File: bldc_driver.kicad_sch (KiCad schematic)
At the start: 100 parts, among them IC1 STSPIN32G4, IC2 AS5047D-ATSM, J2 Conn_01x02_Pin, J3 Conn_01x02_Pin, J4 Conn_01x05_Pin, J4 ST-Link, P1 USB_C_Plug_USB2.0, Q1 NMOS, Q2 NMOS, Q3 NMOS, Q4 NMOS, Q5 NMOS, Q6 NMOS, U1 TCAN332, U2 NJW1933, Y201 Crystal_GND24

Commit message: フットプリント割り当て中
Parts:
- added C3: 10u, Capacitor_SMD:C_1206_3216Metric_Pad1.33x1.80mm_HandSolder, symbol Device:C
- C1: renamed from C7; footprint (none) -> Capacitor_SMD:C_1206_3216Metric_Pad1.33x1.80mm_HandSolder
- C10: renamed from C1; footprint (none) -> Capacitor_SMD:C_0603_1608Metric_Pad1.08x0.95mm_HandSolder
- C11: renamed from C15; footprint (none) -> Capacitor_SMD:C_0603_1608Metric_Pad1.08x0.95mm_HandSolder
- C12: renamed from C2; footprint (none) -> Capacitor_SMD:C_0603_1608Metric_Pad1.08x0.95mm_HandSolder
- C13: renamed from C3; footprint (none) -> Capacitor_SMD:C_0603_1608Metric_Pad1.08x0.95mm_HandSolder
- C14: renamed from C16; footprint (none) -> Capacitor_SMD:C_0603_1608Metric_Pad1.08x0.95mm_HandSolder
- C15: renamed from C10; footprint (none) -> Capacitor_SMD:C_0603_1608Metric_Pad1.08x0.95mm_HandSolder
- C16: renamed from C9; footprint (none) -> Capacitor_SMD:C_0603_1608Metric_Pad1.08x0.95mm_HandSolder
- C17: renamed from C11; footprint (none) -> Capacitor_SMD:C_0603_1608Metric_Pad1.08x0.95mm_HandSolder
- C18: renamed from C12; footprint (none) -> Capacitor_SMD:C_0603_1608Metric_Pad1.08x0.95mm_HandSolder
- C19: renamed from C26; value 1n -> 2.2n; footprint (none) -> Capacitor_SMD:C_0603_1608Metric_Pad1.08x0.95mm_HandSolder
- C2: renamed from C8; footprint (none) -> Capacitor_SMD:C_1206_3216Metric_Pad1.33x1.80mm_HandSolder
- C20: renamed from C27; value 1n -> 2.2n; footprint (none) -> Capacitor_SMD:C_0603_1608Metric_Pad1.08x0.95mm_HandSolder
- C21: renamed from C28; value 1n -> 2.2n; footprint (none) -> Capacitor_SMD:C_0603_1608Metric_Pad1.08x0.95mm_HandSolder
- C22: renamed from C29; value 1n -> 2.2n; footprint (none) -> Capacitor_SMD:C_0603_1608Metric_Pad1.08x0.95mm_HandSolder
- C23: renamed from C30; value 1n -> 2.2n; footprint (none) -> Capacitor_SMD:C_0603_1608Metric_Pad1.08x0.95mm_HandSolder
- C24: renamed from C31; value 1n -> 2.2n; footprint (none) -> Capacitor_SMD:C_0603_1608Metric_Pad1.08x0.95mm_HandSolder
- C25: renamed from C17; footprint (none) -> Capacitor_SMD:C_0603_1608Metric_Pad1.08x0.95mm_HandSolder
- C26: renamed from C20; footprint (none) -> Capacitor_SMD:C_0603_1608Metric_Pad1.08x0.95mm_HandSolder
- C27: renamed from C21; footprint (none) -> Capacitor_SMD:C_0603_1608Metric_Pad1.08x0.95mm_HandSolder
- C28: renamed from C22; footprint (none) -> Capacitor_SMD:C_0603_1608Metric_Pad1.08x0.95mm_HandSolder
- C29: renamed from C23; footprint (none) -> Capacitor_SMD:CP_Elec_10x10
- C30: renamed from C24; footprint (none) -> Capacitor_SMD:CP_Elec_10x10
- C31: renamed from C25; footprint (none) -> Capacitor_SMD:CP_Elec_10x10
- C32: renamed from C19; footprint (none) -> Capacitor_SMD:C_0603_1608Metric_Pad1.08x0.95mm_HandSolder
- C34: footprint Capacitor_SMD:C_0603_1608Metric_Pad1.08x0.95mm_HandSolder -> Capacitor_SMD:C_0402_1005Metric_Pad0.74x0.62mm_HandSolder
- C4: renamed from C14; footprint (none) -> Capacitor_SMD:C_0603_1608Metric_Pad1.08x0.95mm_HandSolder
- C5: renamed from C32; footprint (none) -> Capacitor_SMD:C_0603_1608Metric_Pad1.08x0.95mm_HandSolder
- C6: renamed from C5; footprint (none) -> Capacitor_SMD:C_1206_3216Metric_Pad1.33x1.80mm_HandSolder
- C7: renamed from C4; footprint (none) -> Capacitor_SMD:C_0603_1608Metric_Pad1.08x0.95mm_HandSolder
- C8: renamed from C6; footprint (none) -> Capacitor_SMD:C_0603_1608Metric_Pad1.08x0.95mm_HandSolder
- C9: renamed from C13; footprint (none) -> Capacitor_SMD:C_0603_1608Metric_Pad1.08x0.95mm_HandSolder
- D1: footprint (none) -> sam:RSX101VAM
- D2: renamed from D3; footprint (none) -> Diode_SMD:D_0603_1608Metric_Pad1.05x0.95mm_HandSolder
- D3: renamed from D4; footprint (none) -> Diode_SMD:D_0603_1608Metric_Pad1.05x0.95mm_HandSolder
- D4: renamed from D5; footprint (none) -> Diode_SMD:D_0603_1608Metric_Pad1.05x0.95mm_HandSolder
- D5: renamed from D6; footprint (none) -> Diode_SMD:D_0603_1608Metric_Pad1.05x0.95mm_HandSolder
- IC1: footprint QFN50P900X900X100-65N-D -> stspin32g4:QFN50P900X900X100-65N-D
- IC2: footprint SOP65P640X120-14N -> as5047:SOP65P640X120-14N
- J4: footprint (none) -> Connector_PinHeader_1.27mm:PinHeader_2x05_P1.27mm_Vertical
- L1: value L -> 33u; footprint (none) -> sam:ELL6SH330M
- L2: footprint (none) -> Inductor_SMD:L_0603_1608Metric_Pad1.05x0.95mm_HandSolder
- P1: footprint (none) -> Connector_USB:USB_C_Receptacle_XKB_U262-16XN-4BVC11
- R1: footprint (none) -> Resistor_SMD:R_0603_1608Metric_Pad0.98x0.95mm_HandSolder
- R10: renamed from R22; footprint (none) -> Resistor_SMD:R_0603_1608Metric_Pad0.98x0.95mm_HandSolder
- R11: renamed from R12; footprint (none) -> Resistor_SMD:R_0603_1608Metric_Pad0.98x0.95mm_HandSolder
- R12: renamed from R16; footprint (none) -> Resistor_SMD:R_0603_1608Metric_Pad0.98x0.95mm_HandSolder
- R13: renamed from R21; footprint (none) -> Resistor_SMD:R_0603_1608Metric_Pad0.98x0.95mm_HandSolder
- R14: renamed from R6; footprint (none) -> Resistor_SMD:R_0603_1608Metric_Pad0.98x0.95mm_HandSolder
- R15: renamed from R7; footprint (none) -> Resistor_SMD:R_0603_1608Metric_Pad0.98x0.95mm_HandSolder
- R16: renamed from R13; footprint (none) -> Resistor_SMD:R_0603_1608Metric_Pad0.98x0.95mm_HandSolder
- R17: renamed from R18; footprint (none) -> Resistor_SMD:R_0603_1608Metric_Pad0.98x0.95mm_HandSolder
- R18: renamed from R23; footprint (none) -> Resistor_SMD:R_0603_1608Metric_Pad0.98x0.95mm_HandSolder
- R19: renamed from R14; footprint (none) -> Resistor_SMD:R_2512_6332Metric_Pad1.40x3.35mm_HandSolder
- R2: renamed from R34; footprint (none) -> Resistor_SMD:R_0603_1608Metric_Pad0.98x0.95mm_HandSolder
- R20: renamed from R19; footprint (none) -> Resistor_SMD:R_2512_6332Metric_Pad1.40x3.35mm_HandSolder
- R21: renamed from R24; footprint (none) -> Resistor_SMD:R_2512_6332Metric_Pad1.40x3.35mm_HandSolder
- R22: renamed from R8; footprint (none) -> Resistor_SMD:R_0603_1608Metric_Pad0.98x0.95mm_HandSolder
- R23: renamed from R9; footprint (none) -> Resistor_SMD:R_0603_1608Metric_Pad0.98x0.95mm_HandSolder
- R24: renamed from R25; value R -> 22k; footprint (none) -> Resistor_SMD:R_0603_1608Metric_Pad0.98x0.95mm_HandSolder
- R25: renamed from R27; value R -> 22k; footprint (none) -> Resistor_SMD:R_0603_1608Metric_Pad0.98x0.95mm_HandSolder
- R26: renamed from R29; value R -> 22k; footprint (none) -> Resistor_SMD:R_0603_1608Metric_Pad0.98x0.95mm_HandSolder
- R27: renamed from R31; footprint (none) -> Resistor_SMD:R_0603_1608Metric_Pad0.98x0.95mm_HandSolder
- R28: renamed from R32; footprint (none) -> Resistor_SMD:R_0603_1608Metric_Pad0.98x0.95mm_HandSolder
- R29: renamed from R33; footprint (none) -> Resistor_SMD:R_0603_1608Metric_Pad0.98x0.95mm_HandSolder
- R3: renamed from R2; footprint (none) -> Resistor_SMD:R_0603_1608Metric_Pad0.98x0.95mm_HandSolder
- R30: renamed from R26; value R -> 300; footprint (none) -> Resistor_SMD:R_0603_1608Metric_Pad0.98x0.95mm_HandSolder
- R31: renamed from R28; value R -> 300; footprint (none) -> Resistor_SMD:R_0603_1608Metric_Pad0.98x0.95mm_HandSolder
- R32: renamed from R30; value R -> 300; footprint (none) -> Resistor_SMD:R_0603_1608Metric_Pad0.98x0.95mm_HandSolder
- R33: renamed from R5; footprint (none) -> Resistor_SMD:R_0603_1608Metric_Pad0.98x0.95mm_HandSolder
- R34: renamed from R3; footprint (none) -> Resistor_SMD:R_0603_1608Metric_Pad0.98x0.95mm_HandSolder
- R35: renamed from R4; footprint (none) -> Resistor_SMD:R_0603_1608Metric_Pad0.98x0.95mm_HandSolder
- R4: renamed from R35; footprint (none) -> Resistor_SMD:R_0603_1608Metric_Pad0.98x0.95mm_HandSolder
- R5: renamed from R10; footprint (none) -> Resistor_SMD:R_0603_1608Metric_Pad0.98x0.95mm_HandSolder
- R6: renamed from R15; footprint (none) -> Resistor_SMD:R_0603_1608Metric_Pad0.98x0.95mm_HandSolder
- R7: renamed from R20; footprint (none) -> Resistor_SMD:R_0603_1608Metric_Pad0.98x0.95mm_HandSolder
- R8: renamed from R11; footprint (none) -> Resistor_SMD:R_0603_1608Metric_Pad0.98x0.95mm_HandSolder
- R9: renamed from R17; footprint (none) -> Resistor_SMD:R_0603_1608Metric_Pad0.98x0.95mm_HandSolder
- U1: footprint (none) -> Package_SO:SOIC-8_3.9x4.9mm_P1.27mm
- renumbered C33 to C35, C35 to C36, D7 to D6, J2 to J1, J3 to J2, J4 to J3, Q3 to Q2, Q5 to Q3, Q2 to Q4, Q4 to Q5, R39 to R36, R36 to R37, R37 to R38, R38 to R39
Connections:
- net SPI1_SCK is gone; now on net SPI1_CLK: IC1.54 (PB3)
- net +3V3: now also C25.1, C6.1, C7.1, IC1.1 (REG3V3/VDD), IC2.11 (VDD), IC2.12 (VDD3V), L2.2, U1.3 (VCC)
- net GND: now also C3.2
- net VCC: now also C3.1
- net VDD: no longer C25.1, C6.1, C7.1, IC1.1 (REG3V3/VDD), IC2.11 (VDD), IC2.12 (VDD3V), L2.2, U1.3 (VCC)
- net VDDA renamed +3V3A
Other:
- note added: "Bias and Filter of Current Sensor"
- note removed: "Current Sensors"
- note removed: "LPF"
- moved on the sheet: C2, C206, D1, D202, P1, R34, R35

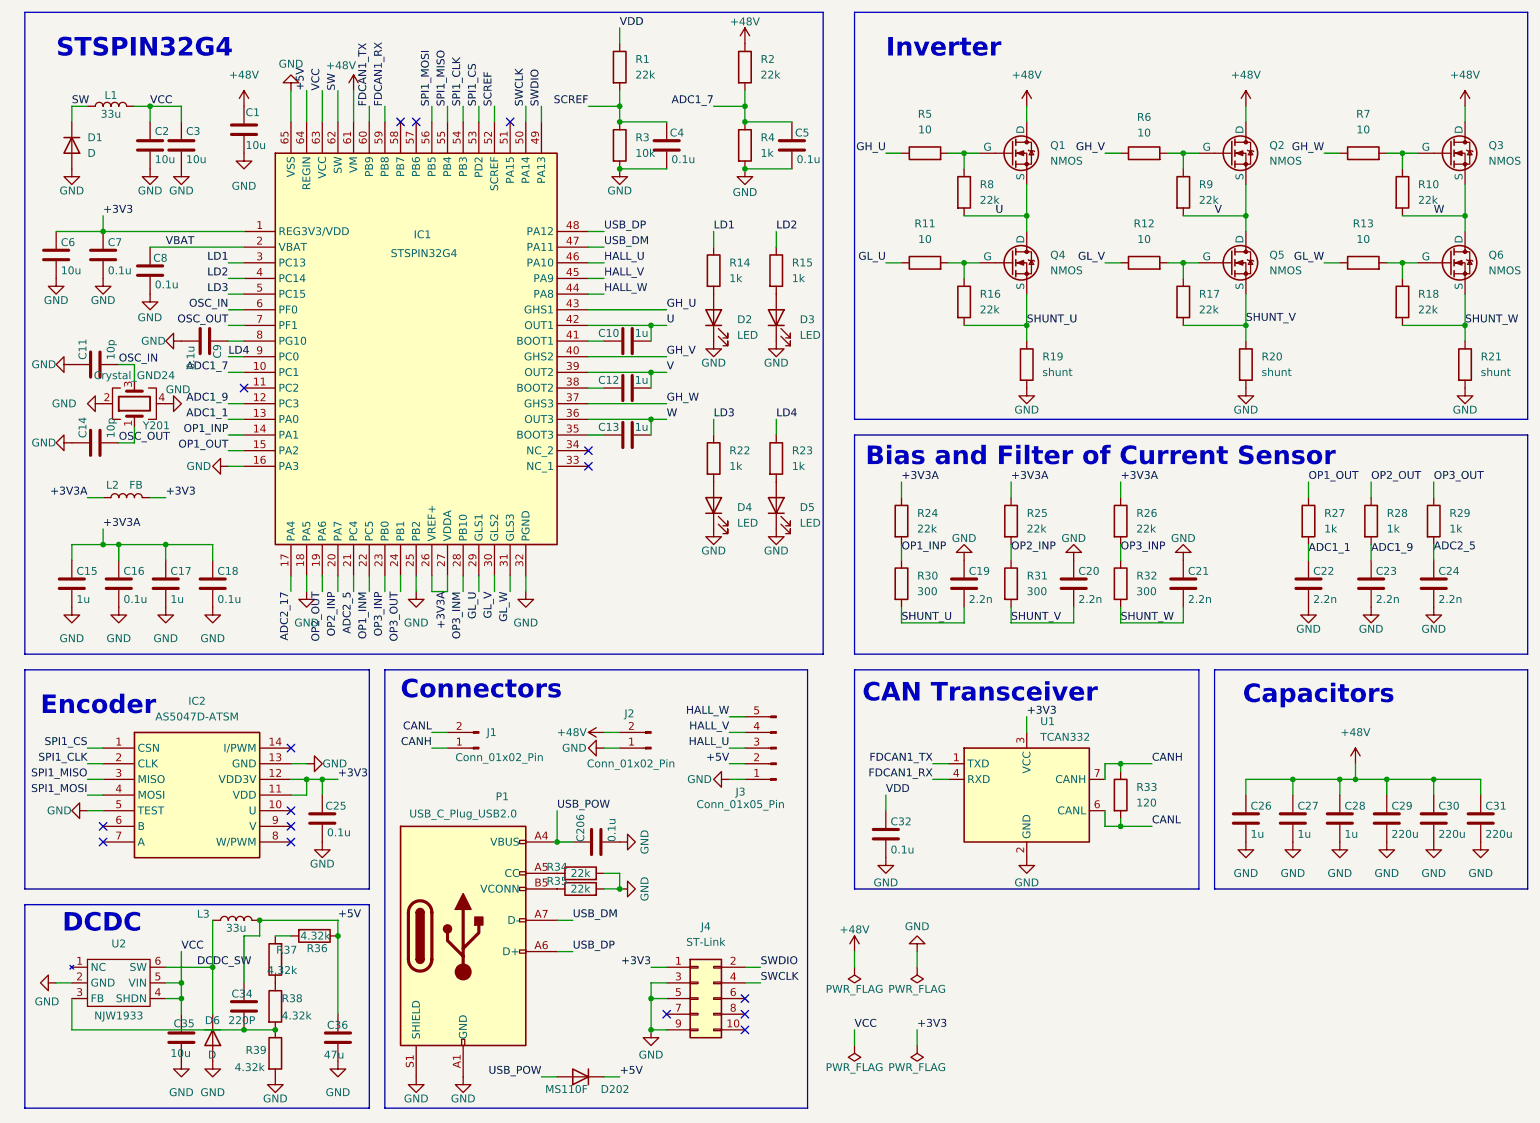
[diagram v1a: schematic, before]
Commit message: 割り当て終了+gitignore追加
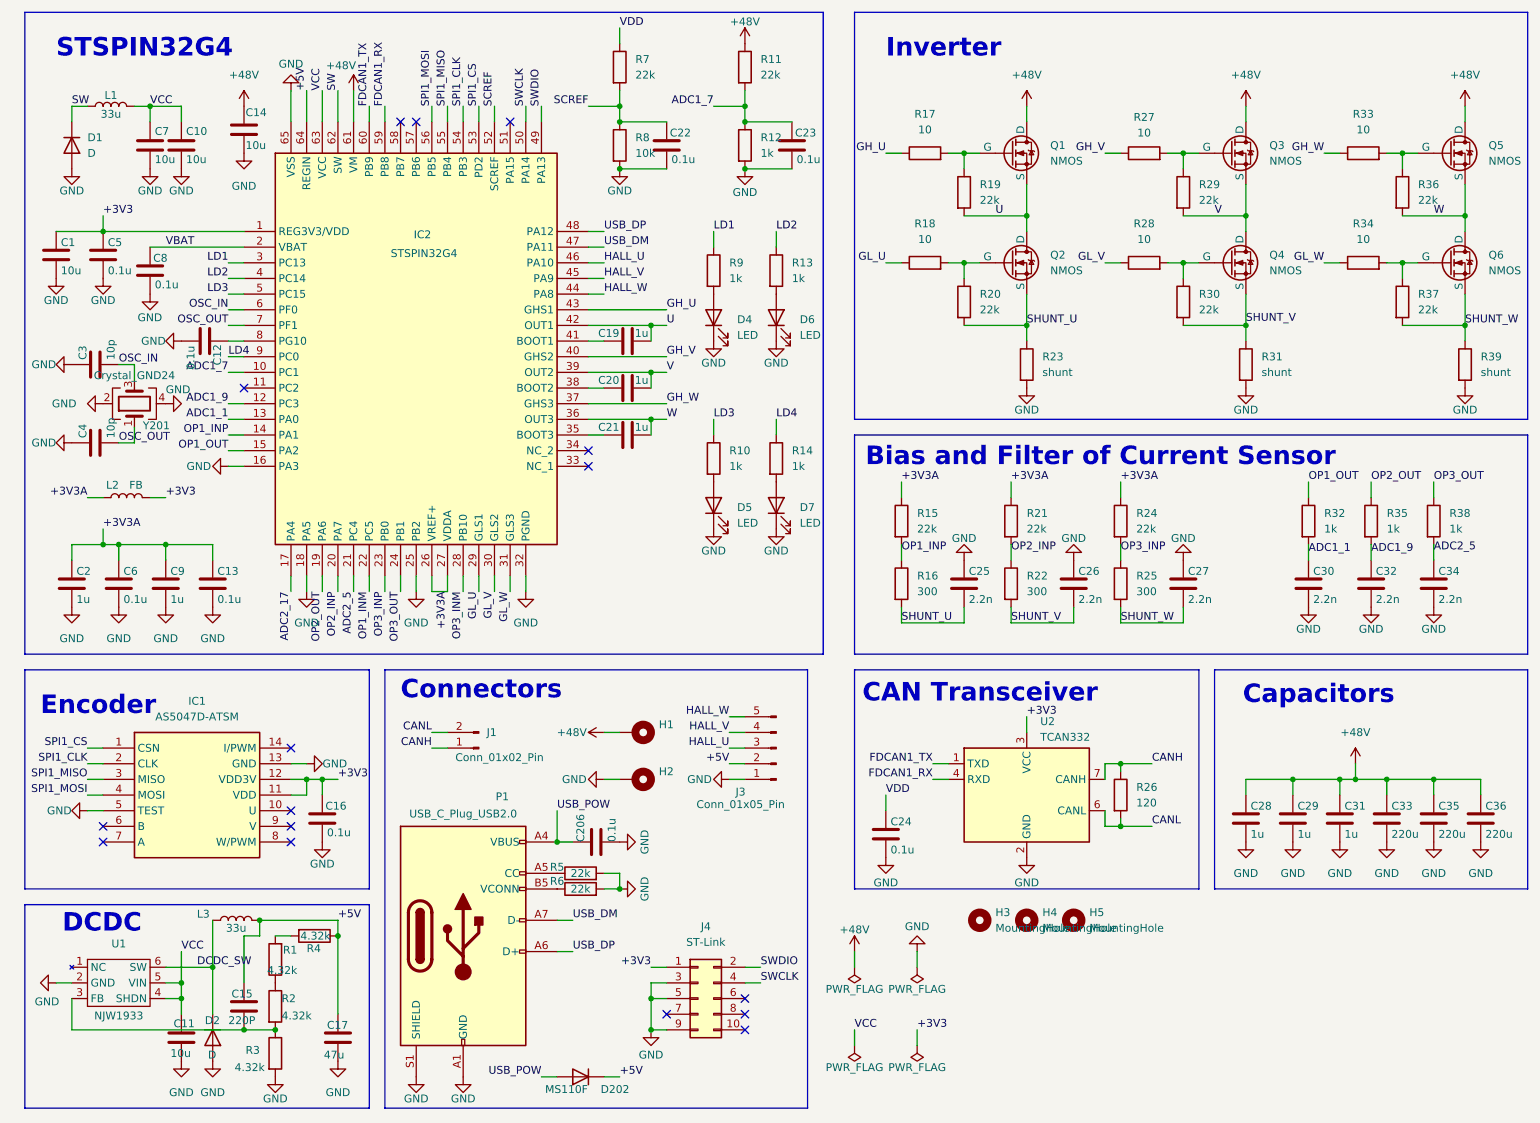
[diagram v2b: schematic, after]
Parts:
- removed J2: Conn_01x02_Pin, symbol Connector:Conn_01x02_Pin
- added H1, H2: MountingHole_Pad, MountingHole:MountingHole_2.5mm_Pad_TopBottom, symbol Mechanical:MountingHole_Pad
- added H3, H4, H5: MountingHole, MountingHole:MountingHole_3.2mm_M3, symbol Mechanical:MountingHole
- J1: footprint (none) -> Connector_JST:JST_XH_S2B-XH-A-1_1x02_P2.50mm_Horizontal
- J3: footprint (none) -> Connector_JST:JST_XH_S5B-XH-A_1x05_P2.50mm_Horizontal
- Q1, Q6: footprint (none) -> sam:SOT8002-1-8
- Q2: renamed from Q4; footprint (none) -> sam:SOT8002-1-8
- Q3: renamed from Q2; footprint (none) -> sam:SOT8002-1-8
- Q4: renamed from Q5; footprint (none) -> sam:SOT8002-1-8
- Q5: renamed from Q3; footprint (none) -> sam:SOT8002-1-8
- renumbered C6 to C1, C3 to C10, C35 to C11, C9 to C12, C18 to C13, C1 to C14, C34 to C15, C25 to C16, C36 to C17, C10 to C19, C15 to C2, C12 to C20, C13 to C21, C4 to C22, C5 to C23, C32 to C24, C19 to C25, C20 to C26, C21 to C27, C26 to C28, C27 to C29, C11 to C3, C22 to C30, C28 to C31, C23 to C32, C29 to C33, C24 to C34, C30 to C35, C31 to C36, C14 to C4, C7 to C5, C16 to C6, C2 to C7, C17 to C9, D6 to D2, D2 to D4, D4 to D5, D3 to D6, D5 to D7, IC2 to IC1, IC1 to IC2, R37 to R1, R22 to R10, R2 to R11, R4 to R12, R15 to R13, R23 to R14, R24 to R15, R30 to R16, R5 to R17, R11 to R18, R8 to R19, R38 to R2, R16 to R20, R25 to R21, R31 to R22, R19 to R23, R26 to R24, R32 to R25, R33 to R26, R6 to R27, R12 to R28, R9 to R29, R39 to R3, R17 to R30, R20 to R31, R27 to R32, R7 to R33, R13 to R34, R28 to R35, R10 to R36, R18 to R37, R29 to R38, R21 to R39, R36 to R4, R34 to R5, R35 to R6, R1 to R7, R3 to R8, R14 to R9, U2 to U1, U1 to U2
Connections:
- net +48V: now also H1.1
- net GND: now also H2.1

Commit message: なんとなく配線できてきた
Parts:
- removed C206: 0.1u, Capacitor_SMD:C_0603_1608Metric_Pad1.08x0.95mm_HandSolder, symbol Device:C
- removed D202: MS110F, bdm:MS110F, symbol Device:D
- removed H1, H2: MountingHole_Pad, MountingHole:MountingHole_2.5mm_Pad_TopBottom, symbol Mechanical:MountingHole_Pad
- removed R1, R4: 4.32k, Resistor_SMD:R_0603_1608Metric_Pad0.98x0.95mm_HandSolder, symbol Device:R
- added H4: MountingHole, MountingHole:MountingHole_3.2mm_M3, symbol Mechanical:MountingHole
- IC2: footprint stspin32g4:QFN50P900X900X100-65N-D -> stspin32g4:QFN50P900X900X100-65N-D-padlong
- J1: footprint Connector_JST:JST_XH_S2B-XH-A-1_1x02_P2.50mm_Horizontal -> Connector_PinHeader_2.54mm:PinHeader_1x02_P2.54mm_Vertical
- J3: footprint Connector_JST:JST_XH_S5B-XH-A_1x05_P2.50mm_Horizontal -> sam:PinHeader_1x05_P1.27mm_Vertical_big
- J4: footprint Connector_PinHeader_1.27mm:PinHeader_2x05_P1.27mm_Vertical -> sam:PinHeader_2x05_P1.27mm_Vertical_big
- R2: value 4.32k -> 10k
- Y201: footprint Crystal:Crystal_SMD_SeikoEpson_FA238V-4Pin_3.2x2.5mm_HandSoldering -> Crystal:Crystal_SMD_SeikoEpson_FA238V-4Pin_3.2x2.5mm
- renumbered H3 to H1, H4 to H2, H5 to H3, R26 to R4
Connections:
- net VDD is gone; now on net +3V3: C24.1, R7.1
- net +5V: now also R2.1
- net ADC1_7: now also C32.1, R35.2; no longer C23.1, R11.2, R12.1
- net ADC1_9: now also C23.1, R11.2, R12.1; no longer C32.1, R35.2
- net OP1_INP: now also R24.2, R25.1; no longer R15.2, R16.1
- net OP3_INP: now also R15.2, R16.1; no longer R24.2, R25.1
- net USB_POW: no longer names the net of P1.A4 (VBUS), P1.A9 (VBUS), P1.B4 (VBUS), P1.B9 (VBUS)
- no-connect marks 16 -> 17
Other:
- moved on the sheet: L3

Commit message: 配線がほとんど終わった
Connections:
- net HALL_U: now also J3.5 (Pin_5); no longer J3.3 (Pin_3)
- net HALL_W: now also J3.3 (Pin_3); no longer J3.5 (Pin_5)
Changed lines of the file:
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@@
     (effects (font (size 1.27 1.27)) (justify left bottom))
   )
-  (label "HALL_W" (at 139.7 129.54 180) (fields_autoplaced)
+  (label "HALL_U" (at 139.7 129.54 180) (fields_autoplaced)
     (effects (font (size 1.27 1.27)) (justify right bottom))
   )
@@
     (effects (font (size 1.27 1.27)) (justify left bottom))
   )
-  (label "HALL_U" (at 139.7 134.62 180) (fields_autoplaced)
+  (label "HALL_W" (at 139.7 134.62 180) (fields_autoplaced)
     (effects (font (size 1.27 1.27)) (justify right bottom))
   )

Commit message: ガーバー吐いた
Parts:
- C15: value 220P -> 330p; footprint Capacitor_SMD:C_0402_1005Metric_Pad0.74x0.62mm_HandSolder -> Capacitor_SMD:C_0603_1608Metric_Pad1.08x0.95mm_HandSolder
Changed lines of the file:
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@@
       (effects (font (size 1.27 1.27)) (justify left))
     )
-    (property "Value" "220P" (at 58.42 178.816 0)
+    (property "Value" "330p" (at 58.42 178.816 0)
       (effects (font (size 1.27 1.27)) (justify left))
     )
-    (property "Footprint" "Capacitor_SMD:C_0402_1005Metric_Pad0.74x0.62mm_HandSolder" (at 61.9252 180.34 0)
+    (property "Footprint" "Capacitor_SMD:C_0603_1608Metric_Pad1.08x0.95mm_HandSolder" (at 61.9252 180.34 0)
       (effects (font (size 1.27 1.27)) hide)
     )

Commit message: 値及びフットプリント修正
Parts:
- added C18: 220p, Capacitor_SMD:C_0402_1005Metric_Pad0.74x0.62mm_HandSolder, symbol Device:C
- C10, C11, C7: footprint Capacitor_SMD:C_1206_3216Metric_Pad1.33x1.80mm_HandSolder -> Capacitor_SMD:C_0805_2012Metric_Pad1.18x1.45mm_HandSolder
- C15: value 330p -> 220p; footprint Capacitor_SMD:C_0603_1608Metric_Pad1.08x0.95mm_HandSolder -> Capacitor_SMD:C_0402_1005Metric_Pad0.74x0.62mm_HandSolder
- C25, C26, C27, C30, C32, C34: value 2.2n -> 1n
- C28, C29, C31: value 1u -> 0.1u
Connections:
- net +5V: now also C18.1
- net at C15.2, R2.2, R3.1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: now also C18.2
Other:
- moved on the sheet: R2, R3
